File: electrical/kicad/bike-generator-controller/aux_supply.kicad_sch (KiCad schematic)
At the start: 21 parts, among them U4 LM5164DDAT

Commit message: feat: establish controller PCB V1 design baseline
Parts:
- added C13: 10uF / 100V, Capacitor_SMD:C_1210_3225Metric_Pad1.33x2.70mm_HandSolder, symbol Device:C
- C10: footprint (none) -> Capacitor_SMD:C_0805_2012Metric_Pad1.18x1.45mm_HandSolder; LCSC (none) -> C107149; MPN (none) -> CC0805KRX7R9BB332; Manufacturer (none) -> Yageo
- C11: footprint (none) -> Capacitor_SMD:C_0805_2012Metric_Pad1.18x1.45mm_HandSolder; LCSC (none) -> C113833; MPN (none) -> CC0805JRNPO9BN820; Manufacturer (none) -> Yageo
- C4, C5: value 2.2uF 100V -> 10uF / 100V; footprint (none) -> Capacitor_SMD:C_1210_3225Metric_Pad1.33x2.70mm_HandSolder; Dielectric (none) -> X7S; LCSC (none) -> C5596909; MPN (none) -> CL32Y106KCVZ4NE; Manufacturer (none) -> Samsung Electro-Mechanics
- C6: value 10uF -> 10uF / 100V; footprint (none) -> Capacitor_THT:CP_Radial_D6.3mm_P2.50mm; MPN (none) -> EEU-FC2A100; Manufacturer (none) -> Panasonic Industry
- C7, C8: footprint (none) -> Capacitor_SMD:C_1210_3225Metric_Pad1.33x2.70mm_HandSolder; LCSC (none) -> C55530; MPN (none) -> CL32B226KOJNNNE; Manufacturer (none) -> Samsung Electro-Mechanics
- C9: footprint (none) -> Capacitor_SMD:C_0805_2012Metric_Pad1.18x1.45mm_HandSolder; LCSC (none) -> C107146; MPN (none) -> CC0805KRX7R9BB222; Manufacturer (none) -> Yageo
- L1: footprint (none) -> Inductor_SMD:L_Coilcraft_MSS1038-XXX; MPN (none) -> MSS1038-473MLC; Manufacturer (none) -> Coilcraft
- R10, R13: footprint (none) -> Resistor_SMD:R_0805_2012Metric_Pad1.20x1.40mm_HandSolder; LCSC (none) -> C114562; MPN (none) -> RC0805FR-07200KL; Manufacturer (none) -> Yageo
- R11: footprint (none) -> Resistor_SMD:R_0805_2012Metric_Pad1.20x1.40mm_HandSolder; LCSC (none) -> C865397; MPN (none) -> RT0805BRD07316KL; Manufacturer (none) -> Yageo
- R12: footprint (none) -> Resistor_SMD:R_0805_2012Metric_Pad1.20x1.40mm_HandSolder; LCSC (none) -> C122537; MPN (none) -> RT0805BRD07100KL; Manufacturer (none) -> Yageo
- R14: footprint (none) -> Resistor_SMD:R_0805_2012Metric_Pad1.20x1.40mm_HandSolder; LCSC (none) -> C126351; MPN (none) -> RC0805FR-0747KL; Manufacturer (none) -> Yageo
- R8: footprint (none) -> Resistor_SMD:R_1206_3216Metric_Pad1.30x1.75mm_HandSolder; LCSC (none) -> C274076; MPN (none) -> RC1206FR-0741K2L; Manufacturer (none) -> Yageo
- R9: footprint (none) -> Resistor_SMD:R_0805_2012Metric_Pad1.20x1.40mm_HandSolder; LCSC (none) -> C107700; MPN (none) -> RC0805FR-071ML; Manufacturer (none) -> Yageo
- U4: footprint Package_SO:SOIC-8-1EP_3.9x4.9mm_P1.27mm_EP2.95x4.9mm_Mask2.71x3.4mm_ThermalVias -> BikeGenerator:SOIC-8-1EP_DDA_EP2.95x4.9mm_6Vias_D0.30mm
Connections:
- net AUX_IN_PROTECTED: now also C13.1
- net GND: now also C13.2

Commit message: wip: checkpoint controller routing before review
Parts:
- removed TP14: AUX_PGOOD, TestPoint:TestPoint_Pad_D1.5mm, symbol Connector:TestPoint
- removed TP15: GND, TestPoint:TestPoint_Pad_D1.5mm, symbol Connector:TestPoint
- C5: renamed from C13; value 10uF / 100V -> 10uF/100V
- C6: value 10uF / 100V -> 10uF/100V
- C7: renamed from C4; value 10uF / 100V -> 10uF/100V
- C8: renamed from C5; value 10uF / 100V -> 10uF/100V
- C9: value 2.2nF 50V -> 2.2nF/50V
- R12: renamed from R8; value 41.2k / 1% -> 41.2k/1%
- R13: renamed from R9; value 1M / 1% -> 1M/1%
- R14: renamed from R10; value 200k / 1% -> 200k/1%
- R16: renamed from R13; value 200k / 1% -> 200k/1%
- R17: renamed from R11; value 316k / 0.1% -> 316k/0.1%
- R18: renamed from R12; value 100k / 0.1% -> 100k/0.1%
- TP12: value AUX_IN -> (none)
- renumbered C11 to C10, C10 to C11, C8 to C12, C7 to C13, R14 to R15, TP13 to TP14
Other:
- moved on the sheet: C10, C11, C12, C13, C5, C6, C7, C8, C9, L1, R12, R13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

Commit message: feat: close controller v1 design and define integrated v2
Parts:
- C5, C7, C8: DC Bias Note (none) -> Approx. 1.39uF effective each at 80V/25C; validate bus over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
- R12: Electrical Requirement (none) -> 41.2k 1%; low-voltage RON pin; connect only to GND; Function (none) -> LM5164 RON programming, approx. 300kHz
- R13: Electrical Requirement (none) -> 1M 1%; >=100V working; >=0.1W (about 4.5mW at 80V input)
- R14: Electrical Requirement (none) -> 200k 1%; >=25V working; >=0.1W (about 0.9mW at 80V input)
- R17: Electrical Requirement (none) -> 316k 0.1%; >=25V working; >=0.1W
- R18: Electrical Requirement (none) -> 100k 0.1%; >=25V working; >=0.1W
- TP12: value (none) -> AUX_IN_PROTECTED
- U4: MPN (none) -> LM5164DDAT; Manufacturer (none) -> Texas Instruments
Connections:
- net AUX_IN_PROTECTED: no longer R12.1
- net GND: now also R12.1
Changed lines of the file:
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@@
+	)
+	(junction
+		(at 114.3 127)
+		(diameter 0)
+		(color 0 0 0 0)
 	)
 	(junction
@@
 	)
 	(junction
-		(at 81.28 81.28)
-		(diameter 0)
-		(color 0 0 0 0)
-	)
-	(junction
 		(at 203.2 127)
 		(diameter 0)
@@
 	(wire
 		(pts
+			(xy 148.59 111.76) (xy 153.67 111.76)
+		)
+		(stroke
+			(width 0)
+			(type default)
+		)
+	)
+	(wire
+		(pts
 			(xy 139.7 86.36) (xy 161.29 86.36)
 		)
@@
 	(wire
 		(pts
-			(xy 81.28 83.82) (xy 81.28 81.28)
-		)
-		(stroke
-			(width 0)
-			(type default)
-		)
-	)
-	(wire
-		(pts
 			(xy 228.6 97.79) (xy 228.6 96.52)
 		)
@@
 	(wire
 		(pts
-			(xy 81.28 91.44) (xy 81.28 111.76)
+			(xy 114.3 119.38) (xy 114.3 127)
 		)
 		(stroke
@@
 	(wire
 		(pts
+			(xy 114.3 127) (xy 124.46 127)
+		)
+		(stroke
+			(width 0)
+			(type default)
+		)
+	)
+	(wire
+		(pts
 			(xy 203.2 76.2) (xy 203.2 88.9)
 		)
@@
 	(wire
 		(pts
-			(xy 49.53 127) (xy 124.46 127)
+			(xy 49.53 127) (xy 114.3 127)
 		)
 		(stroke
@@
 	(wire
 		(pts
-			(xy 81.28 111.76) (xy 114.3 111.76)
-		)
-		(stroke
-			(width 0)
-			(type default)
-		)
-	)
-	(wire
-		(pts
 			(xy 215.9 96.52) (xy 222.25 96.52)
 		)
@@
 		(pts
 			(xy 140.97 93.98) (xy 140.97 111.76)
-		)
-		(stroke
-			(width 0)
-			(type default)
-		)
-	)
-	(wire
-		(pts
-			(xy 148.59 111.76) (xy 151.13 111.76)
 		)
 		(stroke
@@
 	)
 	(label "RON_SET"
-		(at 111.76 111.76 180)
+		(at 114.3 104.14 180)
 		(effects
 			(font
@@
 	(hierarchical_label "AUX_PGOOD"
 		(shape output)
-		(at 151.13 111.76 0)
+		(at 153.67 111.76 0)
 		(effects
 			(font
@@
 			)
 		)
+		(property "DC Bias Note" "Approx. 1.39uF effective each at 80V/25C; validate bus overshoot"
+			(at 68.58 96.52 0)
+			(hide yes)
+			(show_name no)
+			(do_not_autoplace no)
+			(effects
+				(font
+					(size 1.27 1.27)
+				)
+			)
+		)
 		(pin "1"
 		)
@@
 			)
 		)
-		(property "Value" ""
+		(property "Value" "AUX_IN_PROTECTED"
 			(at 41.402 83.312 0)
 			(hide yes)
@@
 			)
 		)
+		(property "Electrical Requirement" "200k 1%; >=25V working; >=0.1W (about 0.9mW at 80V input)"
+			(at 96.52 97.79 0)
+			(hide yes)
+			(show_name no)
+			(do_not_autoplace no)
+			(effects
+				(font
+					(size 1.27 1.27)
+				)
+			)
+		)
 		(pin "2"
 		)
@@
 			)
 		)
-		(property "Datasheet" "https://www.ti.com/lit/ds/symlink/lm5164.pdf?ts=1598311864250&ref_url=https%253A%252F%252Fwww.ti.com%252Fproduct%252FLM5164%253FHQS%253DTI-null-null-octopart-df-pf-null-wwe"
+		(property "Datasheet" "https://www.ti.com/lit/ds/symlink/lm5164.pdf"
 			(at 127 88.9 0)
 			(hide yes)
@@
 		)
 		(property "Description" "1A synchronous buck converter with ultra-low IQ, 6V - 100V input, adjustable output voltage, HSOP-8"
+			(at 127 88.9 0)
+			(hide yes)
+			(show_name no)
+			(do_not_autoplace no)
+			(effects
+				(font
+					(size 1.27 1.27)
+				)
+			)
+		)
+		(property "Manufacturer" "Texas Instruments"
+			(at 127 88.9 0)
+			(hide yes)
+			(show_name no)
+			(do_not_autoplace no)
+			(effects
+				(font
+					(size 1.27 1.27)
+				)
+			)
+		)
+		(property "MPN" "LM5164DDAT"
 			(at 127 88.9 0)
 			(hide yes)
@@
 			)
 		)
+		(property "Electrical Requirement" "1M 1%; >=100V working; >=0.1W (about 4.5mW at 80V input)"
+			(at 96.52 85.09 0)
+			(hide yes)
+			(show_name no)
+			(do_not_autoplace no)
+			(effects
+				(font
+					(size 1.27 1.27)
+				)
+			)
+		)
 		(pin "2"
 		)
@@
 			)
 		)
+		(property "Electrical Requirement" "100k 0.1%; >=25V working; >=0.1W"
+			(at 203.2 115.57 0)
+			(hide yes)
+			(show_name no)
+			(do_not_autoplace no)
+			(effects
+				(font
+					(size 1.27 1.27)
+				)
+			)
+		)
 		(pin "2"
 		)
@@
 		)
 		(property "Dielectric" "X7S"
+			(at 30.48 96.52 0)
+			(hide yes)
+			(show_name no)
+			(do_not_autoplace no)
+			(effects
+				(font
+					(size 1.27 1.27)
+				)
+			)
+		)
+		(property "DC Bias Note" "Approx. 1.39uF effective each at 80V/25C; validate bus overshoot"
 			(at 30.48 96.52 0)
 			(hide yes)
@@
 	(symbol
 		(lib_id "Device:R")
-		(at 81.28 87.63 0)
+		(at 114.3 115.57 180)
 		(unit 1)
 		(body_style 1)
@@
 		(dnp no)
 		(property "Reference" "R12"
-			(at 85.09 86.36 0)
+			(at 110.49 116.84 0)
 			(show_name no)
 			(do_not_autoplace no)
@@
 		)
 		(property "Value" "41.2k/1%"
-			(at 89.154 88.9 0)
+			(at 106.426 114.3 0)
 			(show_name no)
 			(do_not_autoplace no)
@@
 		)
 		(property "Footprint" "Resistor_SMD:R_1206_3216Metric_Pad1.30x1.75mm_HandSolder"
-			(at 81.28 87.63 0)
+			(at 114.3 115.57 0)
 			(hide yes)
 			(show_name no)
@@
 		)
 		(property "Datasheet" "https://www.yageo.com/upload/media/product/productsearch/datasheet/rchip/PYu-RC_Group_51_RoHS_L_16.pdf"
-			(at 81.28 87.63 0)
+			(at 114.3 115.57 0)
 			(hide yes)
 			(show_name no)
@@
 		)
 		(property "Description" "Resistor"
-			(at 81.28 87.63 0)
+			(at 114.3 115.57 0)
 			(hide yes)
 			(show_name no)
@@
 		)
 		(property "Manufacturer" "Yageo"
-			(at 81.28 87.63 0)
+			(at 114.3 115.57 0)
 			(hide yes)
 			(show_name no)
@@
 		)
 		(property "MPN" "RC1206FR-0741K2L"
-			(at 81.28 87.63 0)
+			(at 114.3 115.57 0)
 			(hide yes)
 			(show_name no)
@@
 		)
 		(property "LCSC" "C274076"
-			(at 81.28 87.63 0)
+			(at 114.3 115.57 0)
+			(hide yes)
+			(show_name no)
+			(do_not_autoplace no)
+			(effects
+				(font
+					(size 1.27 1.27)
+				)
+			)
+		)
+		(property "Function" "LM5164 RON programming, approx. 300kHz"
+			(at 114.3 115.57 0)
+			(hide yes)
+			(show_name no)
+			(do_not_autoplace no)
+			(effects
+				(font
+					(size 1.27 1.27)
+				)
+			)
+		)
+		(property "Electrical Requirement" "41.2k 1%; low-voltage RON pin; connect only to GND"
+			(at 114.3 115.57 0)
 			(hide yes)
 			(show_name no)
@@
 			)
 		)
+		(property "DC Bias Note" "Approx. 1.39uF effective each at 80V/25C; validate bus overshoot"
+			(at 55.88 96.52 0)
+			(hide yes)
+			(show_name no)
+			(do_not_autoplace no)
+			(effects
+				(font
+					(size 1.27 1.27)
+				)
+			)
+		)
 		(pin "2"
 		)
@@
 			(at 203.2 92.71 0)
 			(hide yes)
+			(show_name no)
+			(do_not_autoplace no)
+			(effects
+				(font
+					(size 1.27 1.27)
+				)
+			)
+		)
+		(property "Electrical Requirement" "316k 0.1%; >=25V working; >=0.1W"
+			(at 203.2 92.71 0)
+			(hide yes)

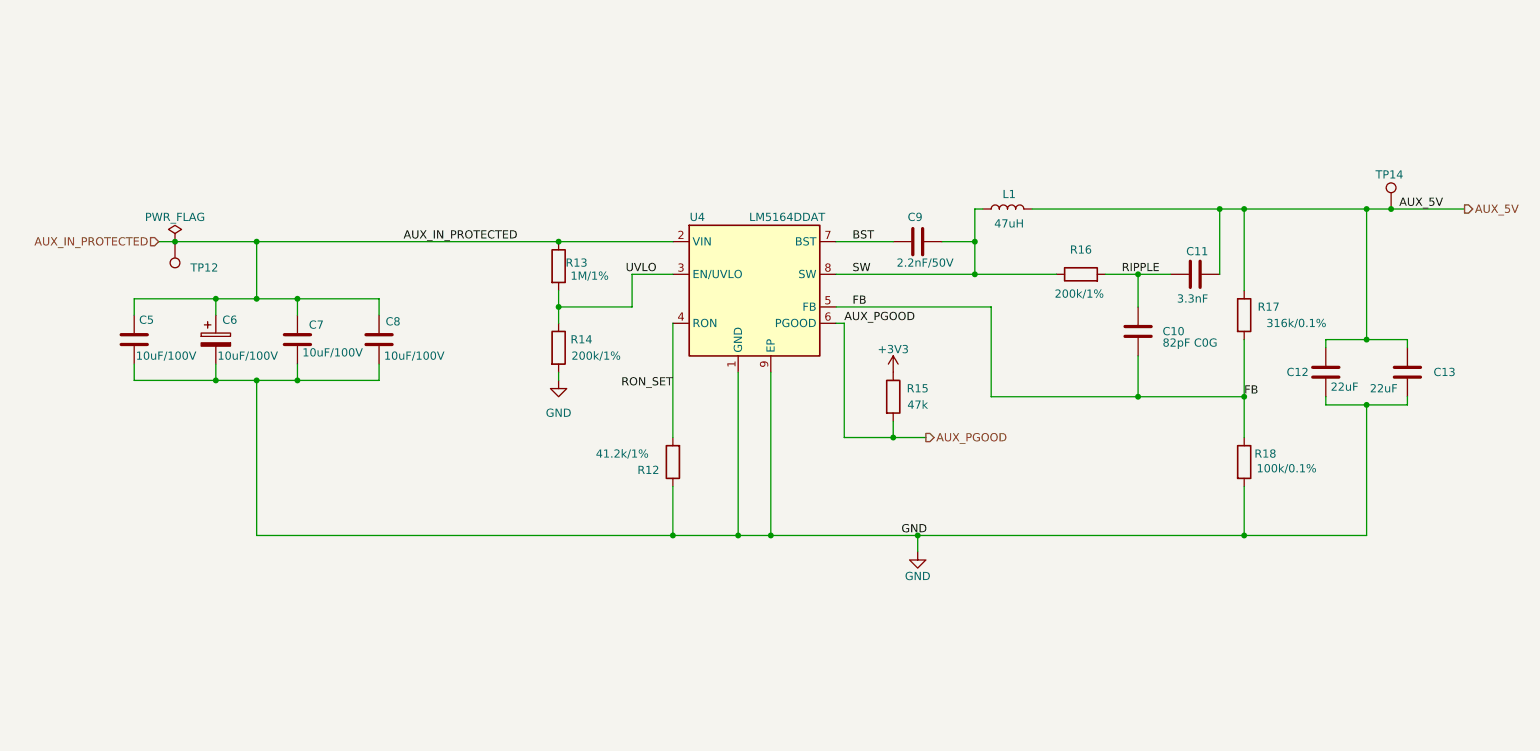
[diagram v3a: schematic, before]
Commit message: feat(controller): finalize V1 design and sourcing
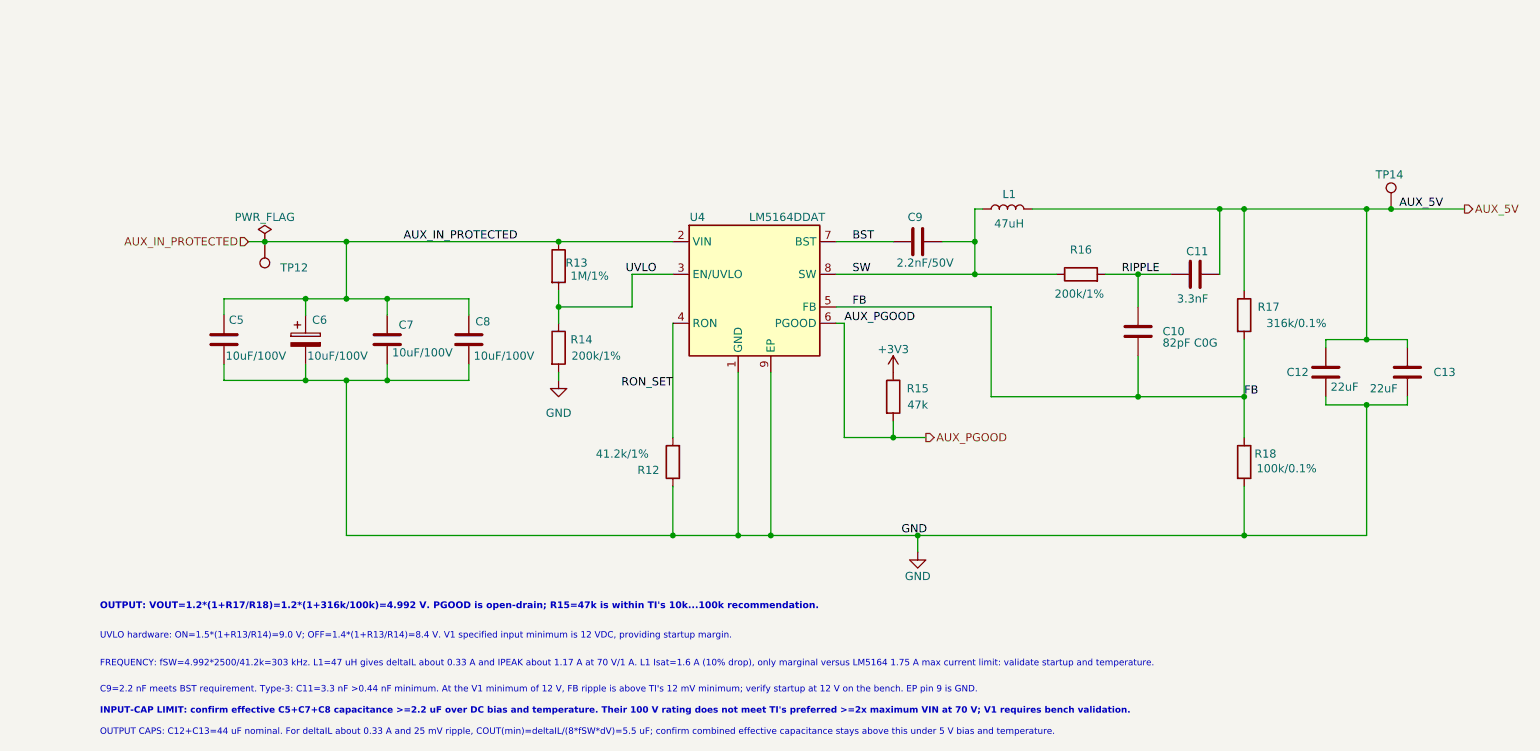
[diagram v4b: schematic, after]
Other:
- note added: "C9=2.2 nF meets BST requirement. Type-3: C11=3.3 nF >0.44 nF minimum. At the V1 minimum of 12 V, FB ripple is above TI's 12 mV minimum; verify startup at 12 V on the bench. EP pin 9 is GND."
- note added: "FREQUENCY: fSW=4.992*2500/41.2k=303 kHz. L1=47 uH gives deltaIL about 0.33 A and IPEAK about 1.17 A at 70 V/1 A. L1 Isat=1.6 A (10% drop), only marginal versus LM5164 1.75 A max current limit: validate startup and temperature."
- note added: "INPUT-CAP LIMIT: confirm effective C5+C7+C8 capacitance >=2.2 uF over DC bias and temperature. Their 100 V rating does not meet TI's preferred >=2x maximum VIN at 70 V; V1 requires bench validation."
- note added: "OUTPUT CAPS: C12+C13=44 uF nominal. For deltaIL about 0.33 A and 25 mV ripple, COUT(min)=deltaIL/(8*fSW*dV)=5.5 uF; confirm combined effective capacitance stays above this under 5 V bias and temperature."
- note added: "OUTPUT: VOUT=1.2*(1+R17/R18)=1.2*(1+316k/100k)=4.992 V. PGOOD is open-drain; R15=47k is within TI's 10k...100k recommendation."
- note added: "UVLO hardware: ON=1.5*(1+R13/R14)=9.0 V; OFF=1.4*(1+R13/R14)=8.4 V. V1 specified input minimum is 12 VDC, providing startup margin."
- moved on the sheet: C5, C6, C7, C8, TP12
